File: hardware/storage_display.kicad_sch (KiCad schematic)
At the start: 0 parts

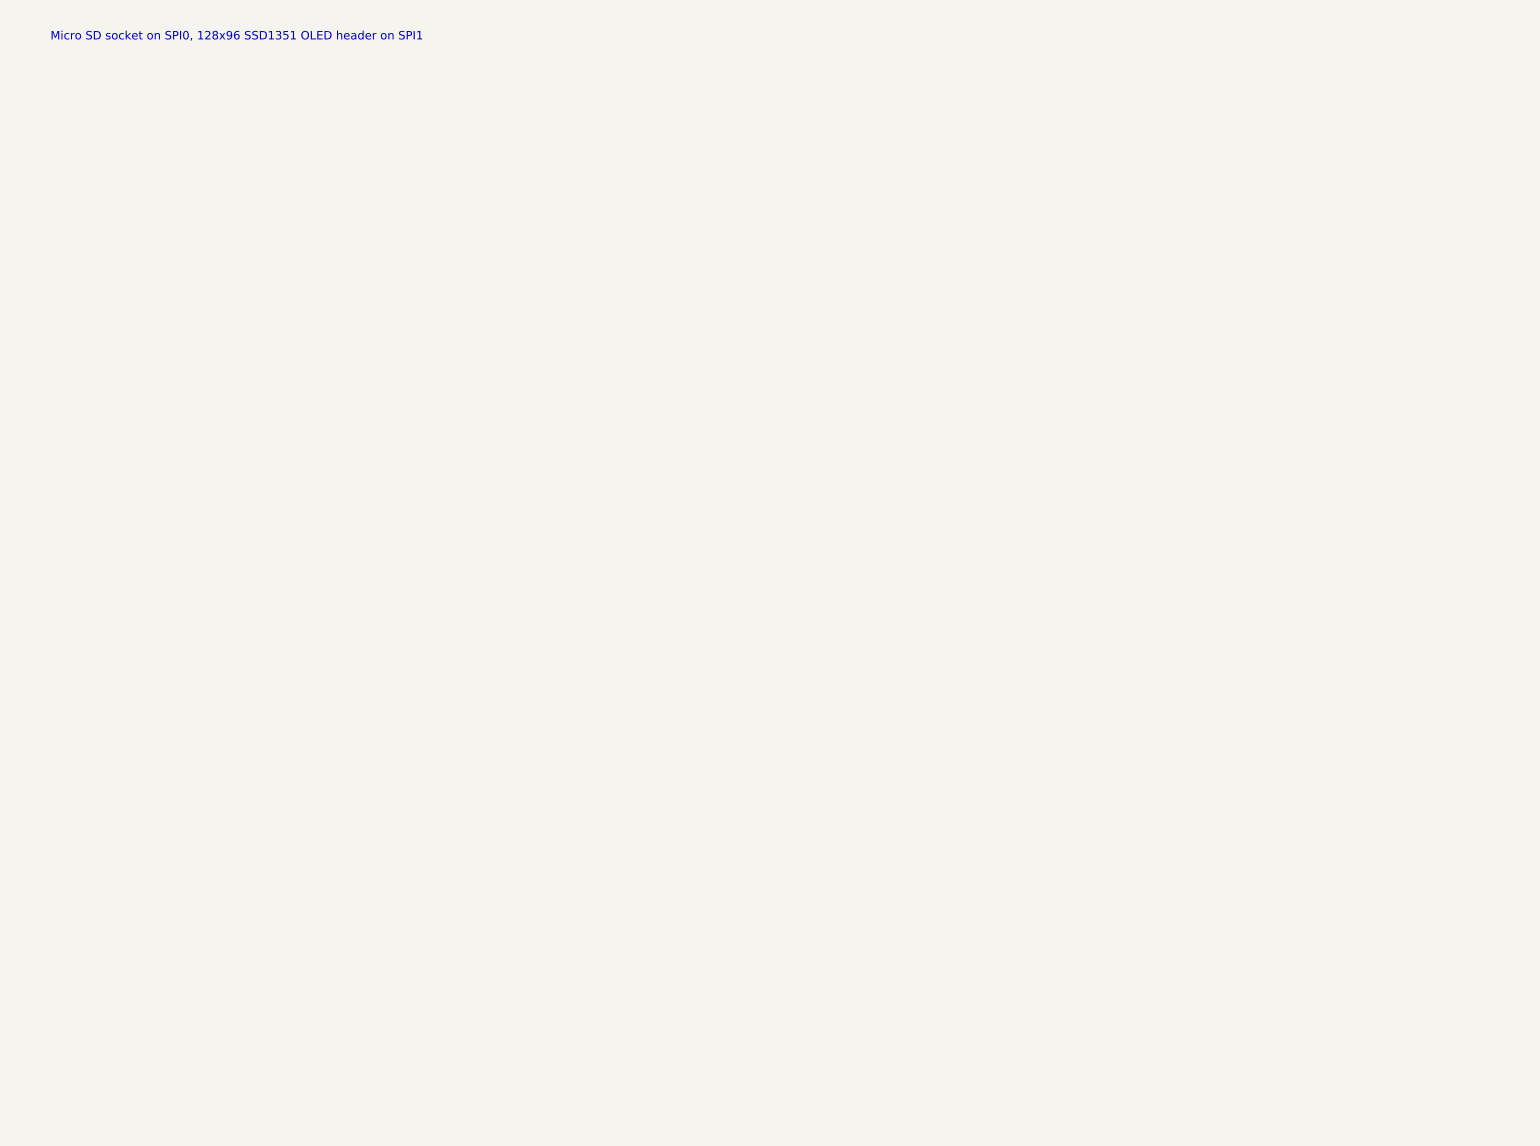
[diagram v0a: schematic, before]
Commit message: Remaining sheets: power, SD and display, WiFi, audio, joystick; ERC clean
- Power: Schottky diode-OR of edge +5V and USB VBUS (card runs from the
  2068/expansion bus, USB alone, or both), two TLV1117LV33 LDOs, bulk caps
- SD: Hirose DM3AT in SPI mode with series R, pull-ups, card detect to STAT
- OLED: 7-pin header (Waveshare 1.27in 128x96 SSD1351) on SPI1
- WiFi: ESP32-C3-WROOM-02 on UART, EN/boot from CTL, IO8 pull-up
- Audio: PWM low-pass, 2068 SOUND mix, MCP6002 buffers, 3.5 mm jack
- Joystick: DE-9 Kempston with pull-ups, series R, optional +5V jumper
- Memory sheet: activity LED on CTL bit 6
- Docs: power decision updated

Co-Authored-By: Claude Fable 5.1 <noreply@anthropic.com>
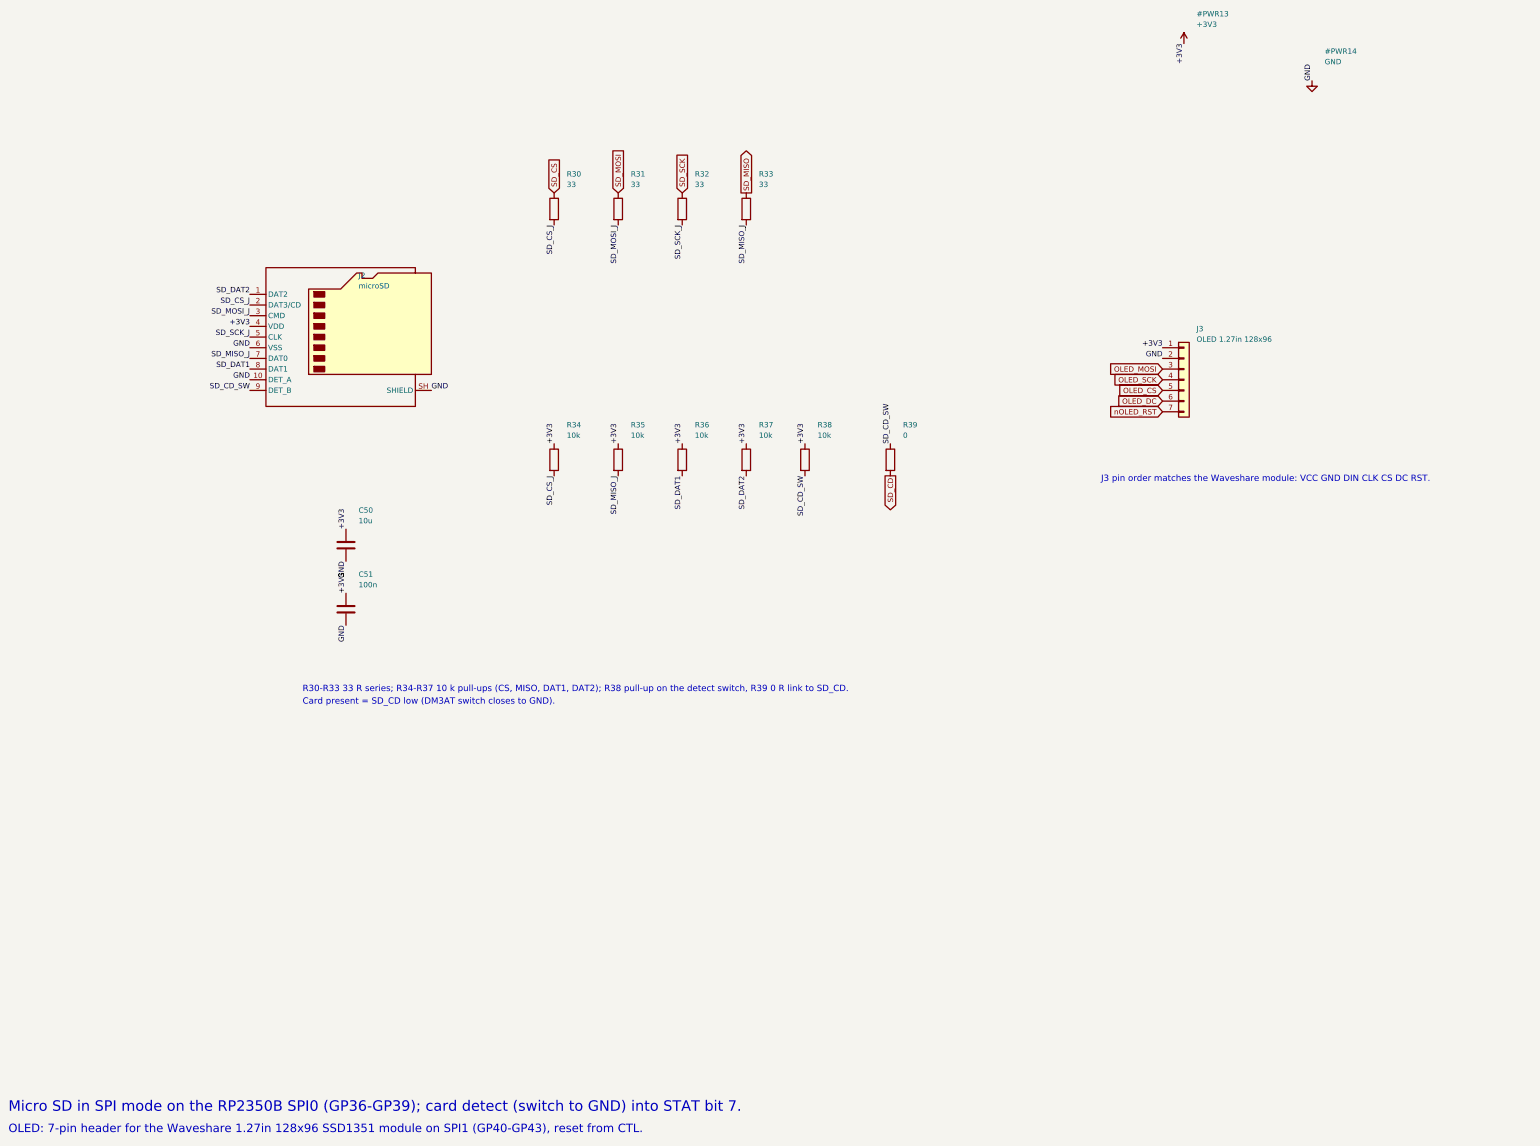
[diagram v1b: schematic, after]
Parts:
- added C50: 10u, Capacitor_SMD:C_0805_2012Metric, symbol Device:C
- added C51: 100n, Capacitor_SMD:C_0603_1608Metric, symbol Device:C
- added J2: microSD, Connector_Card:microSD_HC_Hirose_DM3AT-SF-PEJM5, symbol Connector:Micro_SD_Card_Det_Hirose_DM3AT
- added J3: OLED 1.27in 128x96, Connector_PinHeader_2.54mm:PinHeader_1x07_P2.54mm_Vertical, symbol Connector_Generic:Conn_01x07
- added R30, R31, R32, R33: 33, Resistor_SMD:R_0603_1608Metric, symbol Device:R
- added R34, R35, R36, R37, R38: 10k, Resistor_SMD:R_0603_1608Metric, symbol Device:R
- added R39: 0, Resistor_SMD:R_0603_1608Metric, symbol Device:R
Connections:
- new net +3V3: C50.1, C51.1, J2.4 (VDD), J3.1 (Pin_1), R34.1, R35.1, R36.1, R37.1, R38.1
- new net GND: C50.2, C51.2, J2.10 (DET_A), J2.6 (VSS), J2.SH (SHIELD), J3.2 (Pin_2)
- new net OLED_CS: J3.5 (Pin_5)
- new net OLED_DC: J3.6 (Pin_6)
- new net OLED_MOSI: J3.3 (Pin_3)
- new net OLED_SCK: J3.4 (Pin_4)
- new net SD_CD: R39.2
- new net SD_CD_SW: J2.9 (DET_B), R38.2, R39.1
- new net SD_CS: R30.1
- new net SD_CS_J: J2.2 (DAT3/CD), R30.2, R34.2
- new net SD_DAT1: J2.8 (DAT1), R36.2
- new net SD_DAT2: J2.1 (DAT2), R37.2
- new net SD_MISO: R33.1
- new net SD_MISO_J: J2.7 (DAT0), R33.2, R35.2
- new net SD_MOSI: R31.1
- new net SD_MOSI_J: J2.3 (CMD), R31.2
- new net SD_SCK: R32.1
- new net SD_SCK_J: J2.5 (CLK), R32.2
- new net nOLED_RST: J3.7 (Pin_7)
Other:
- note added: "Card present = SD_CD low (DM3AT switch closes to GND)."
- note added: "J3 pin order matches the Waveshare module: VCC GND DIN CLK CS DC RST."
- note added: "Micro SD in SPI mode on the RP2350B SPI0 (GP36-GP39); card detect (switch to GND) into STAT bit 7."
- note added: "OLED: 7-pin header for the Waveshare 1.27in 128x96 SSD1351 module on SPI1 (GP40-GP43), reset from CTL."
- note added: "R30-R33 33 R series; R34-R37 10 k pull-ups (CS, MISO, DAT1, DAT2); R38 pull-up on the detect switch, R39 0 R link to SD_CD."
- note removed: "Micro SD socket on SPI0, 128x96 SSD1351 OLED header on SPI1"

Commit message: BOM pass: LCSC and MPN fields on every part, JLCPCB BOM export
- scripts/parts.py: part table looked up 2026-09-16; schlib stamps fields
- substitutions for stock: 74HC273PW, 74LVC139PW, TI LVC04/08/126/574/1G86,
  33R USB series, XKB TS-1187A switches, Panasonic polymer 220uF, B5819W
- bom/: JLCPCB-format and full BOM CSVs

Co-Authored-By: Claude Fable 5.1 <noreply@anthropic.com>
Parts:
- C50: LCSC (none) -> C15850; MPN (none) -> CL21A106KAYNNNE
- C51: LCSC (none) -> C14663; MPN (none) -> CC0603KRX7R9BB104
- J2: LCSC (none) -> C114218; MPN (none) -> DM3AT-SF-PEJM5
- J3: LCSC (none) -> C2337; MPN (none) -> 2.54-1x40P (cut to 7)
- R30, R31, R32, R33: LCSC (none) -> C23140; MPN (none) -> 0603WAF330JT5E
- R34, R35, R36, R37, R38: LCSC (none) -> C25804; MPN (none) -> 0603WAF1002T5E
- R39: LCSC (none) -> C21189; MPN (none) -> 0603WAF0000T5E
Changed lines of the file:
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@@
     (property "Datasheet" "" (at 100.33 100.33 0) (effects (font (size 1.27 1.27)) (justify left) (hide yes)))
     (property "Description" "" (at 100.33 100.33 0) (effects (font (size 1.27 1.27)) (justify left) (hide yes)))
+    (property "MPN" "DM3AT-SF-PEJM5" (at 100.33 100.33 0) (effects (font (size 1.27 1.27)) (justify left) (hide yes)))
+    (property "LCSC" "C114218" (at 100.33 100.33 0) (effects (font (size 1.27 1.27)) (justify left) (hide yes)))
     (pin "1")
     (pin "2")
@@
     (property "Datasheet" "" (at 149.86 69.85 0) (effects (font (size 1.27 1.27)) (justify left) (hide yes)))
     (property "Description" "" (at 149.86 69.85 0) (effects (font (size 1.27 1.27)) (justify left) (hide yes)))
+    (property "MPN" "0603WAF330JT5E" (at 149.86 69.85 0) (effects (font (size 1.27 1.27)) (justify left) (hide yes)))
+    (property "LCSC" "C23140" (at 149.86 69.85 0) (effects (font (size 1.27 1.27)) (justify left) (hide yes)))
     (pin "1")
     (pin "2")
@@
     (property "Datasheet" "" (at 165.1 69.85 0) (effects (font (size 1.27 1.27)) (justify left) (hide yes)))
     (property "Description" "" (at 165.1 69.85 0) (effects (font (size 1.27 1.27)) (justify left) (hide yes)))
+    (property "MPN" "0603WAF330JT5E" (at 165.1 69.85 0) (effects (font (size 1.27 1.27)) (justify left) (hide yes)))
+    (property "LCSC" "C23140" (at 165.1 69.85 0) (effects (font (size 1.27 1.27)) (justify left) (hide yes)))
     (pin "1")
     (pin "2")
@@
     (property "Datasheet" "" (at 180.34 69.85 0) (effects (font (size 1.27 1.27)) (justify left) (hide yes)))
     (property "Description" "" (at 180.34 69.85 0) (effects (font (size 1.27 1.27)) (justify left) (hide yes)))
+    (property "MPN" "0603WAF330JT5E" (at 180.34 69.85 0) (effects (font (size 1.27 1.27)) (justify left) (hide yes)))
+    (property "LCSC" "C23140" (at 180.34 69.85 0) (effects (font (size 1.27 1.27)) (justify left) (hide yes)))
     (pin "1")
     (pin "2")
@@
     (property "Datasheet" "" (at 195.58 69.85 0) (effects (font (size 1.27 1.27)) (justify left) (hide yes)))
     (property "Description" "" (at 195.58 69.85 0) (effects (font (size 1.27 1.27)) (justify left) (hide yes)))
+    (property "MPN" "0603WAF330JT5E" (at 195.58 69.85 0) (effects (font (size 1.27 1.27)) (justify left) (hide yes)))
+    (property "LCSC" "C23140" (at 195.58 69.85 0) (effects (font (size 1.27 1.27)) (justify left) (hide yes)))
     (pin "1")
     (pin "2")
@@
     (property "Datasheet" "" (at 149.86 129.54 0) (effects (font (size 1.27 1.27)) (justify left) (hide yes)))
     (property "Description" "" (at 149.86 129.54 0) (effects (font (size 1.27 1.27)) (justify left) (hide yes)))
+    (property "MPN" "0603WAF1002T5E" (at 149.86 129.54 0) (effects (font (size 1.27 1.27)) (justify left) (hide yes)))
+    (property "LCSC" "C25804" (at 149.86 129.54 0) (effects (font (size 1.27 1.27)) (justify left) (hide yes)))
     (pin "1")
     (pin "2")
@@
     (property "Datasheet" "" (at 165.1 129.54 0) (effects (font (size 1.27 1.27)) (justify left) (hide yes)))
     (property "Description" "" (at 165.1 129.54 0) (effects (font (size 1.27 1.27)) (justify left) (hide yes)))
+    (property "MPN" "0603WAF1002T5E" (at 165.1 129.54 0) (effects (font (size 1.27 1.27)) (justify left) (hide yes)))
+    (property "LCSC" "C25804" (at 165.1 129.54 0) (effects (font (size 1.27 1.27)) (justify left) (hide yes)))
     (pin "1")
     (pin "2")
@@
     (property "Datasheet" "" (at 180.34 129.54 0) (effects (font (size 1.27 1.27)) (justify left) (hide yes)))
     (property "Description" "" (at 180.34 129.54 0) (effects (font (size 1.27 1.27)) (justify left) (hide yes)))
+    (property "MPN" "0603WAF1002T5E" (at 180.34 129.54 0) (effects (font (size 1.27 1.27)) (justify left) (hide yes)))
+    (property "LCSC" "C25804" (at 180.34 129.54 0) (effects (font (size 1.27 1.27)) (justify left) (hide yes)))
     (pin "1")
     (pin "2")
@@
     (property "Datasheet" "" (at 195.58 129.54 0) (effects (font (size 1.27 1.27)) (justify left) (hide yes)))
     (property "Description" "" (at 195.58 129.54 0) (effects (font (size 1.27 1.27)) (justify left) (hide yes)))
+    (property "MPN" "0603WAF1002T5E" (at 195.58 129.54 0) (effects (font (size 1.27 1.27)) (justify left) (hide yes)))
+    (property "LCSC" "C25804" (at 195.58 129.54 0) (effects (font (size 1.27 1.27)) (justify left) (hide yes)))
     (pin "1")
     (pin "2")
@@
     (property "Datasheet" "" (at 209.55 129.54 0) (effects (font (size 1.27 1.27)) (justify left) (hide yes)))
     (property "Description" "" (at 209.55 129.54 0) (effects (font (size 1.27 1.27)) (justify left) (hide yes)))
+    (property "MPN" "0603WAF1002T5E" (at 209.55 129.54 0) (effects (font (size 1.27 1.27)) (justify left) (hide yes)))
+    (property "LCSC" "C25804" (at 209.55 129.54 0) (effects (font (size 1.27 1.27)) (justify left) (hide yes)))
     (pin "1")
     (pin "2")
@@
     (property "Datasheet" "" (at 229.87 129.54 0) (effects (font (size 1.27 1.27)) (justify left) (hide yes)))
     (property "Description" "" (at 229.87 129.54 0) (effects (font (size 1.27 1.27)) (justify left) (hide yes)))
+    (property "MPN" "0603WAF0000T5E" (at 229.87 129.54 0) (effects (font (size 1.27 1.27)) (justify left) (hide yes)))
+    (property "LCSC" "C21189" (at 229.87 129.54 0) (effects (font (size 1.27 1.27)) (justify left) (hide yes)))
     (pin "1")
     (pin "2")
@@
     (property "Datasheet" "" (at 100.33 149.86 0) (effects (font (size 1.27 1.27)) (justify left) (hide yes)))
     (property "Description" "" (at 100.33 149.86 0) (effects (font (size 1.27 1.27)) (justify left) (hide yes)))
+    (property "MPN" "CL21A106KAYNNNE" (at 100.33 149.86 0) (effects (font (size 1.27 1.27)) (justify left) (hide yes)))
+    (property "LCSC" "C15850" (at 100.33 149.86 0) (effects (font (size 1.27 1.27)) (justify left) (hide yes)))
     (pin "1")
     (pin "2")
@@
     (property "Datasheet" "" (at 100.33 165.1 0) (effects (font (size 1.27 1.27)) (justify left) (hide yes)))
     (property "Description" "" (at 100.33 165.1 0) (effects (font (size 1.27 1.27)) (justify left) (hide yes)))
+    (property "MPN" "CC0603KRX7R9BB104" (at 100.33 165.1 0) (effects (font (size 1.27 1.27)) (justify left) (hide yes)))
+    (property "LCSC" "C14663" (at 100.33 165.1 0) (effects (font (size 1.27 1.27)) (justify left) (hide yes)))
     (pin "1")
     (pin "2")
@@
     (property "Datasheet" "" (at 299.72 110.49 0) (effects (font (size 1.27 1.27)) (justify left) (hide yes)))
     (property "Description" "" (at 299.72 110.49 0) (effects (font (size 1.27 1.27)) (justify left) (hide yes)))
-    (pin "1")
-    (pin "2")
+    (property "MPN" "2.54-1x40P (cut to 7)" (at 299.72 110.49 0) (effects (font (size 1.27 1.27)) (justify left) (hide yes)))
+    (property "LCSC" "C2337" (at 299.72 110.49 0) (effects (font (size 1.27 1.27)) (justify left) (hide yes)))
+    (pin "1")
+    (pin "2")
